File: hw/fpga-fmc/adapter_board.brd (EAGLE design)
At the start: 69 x 84 mm, 57 parts, among them J1 5569262-1, J2 ASP-134488-01, U1 ADM3066E, U2 ADM3066E, U3 ADM3066E, U4 ADM3066E, U5 ADM3066E, U6 ADM3066E

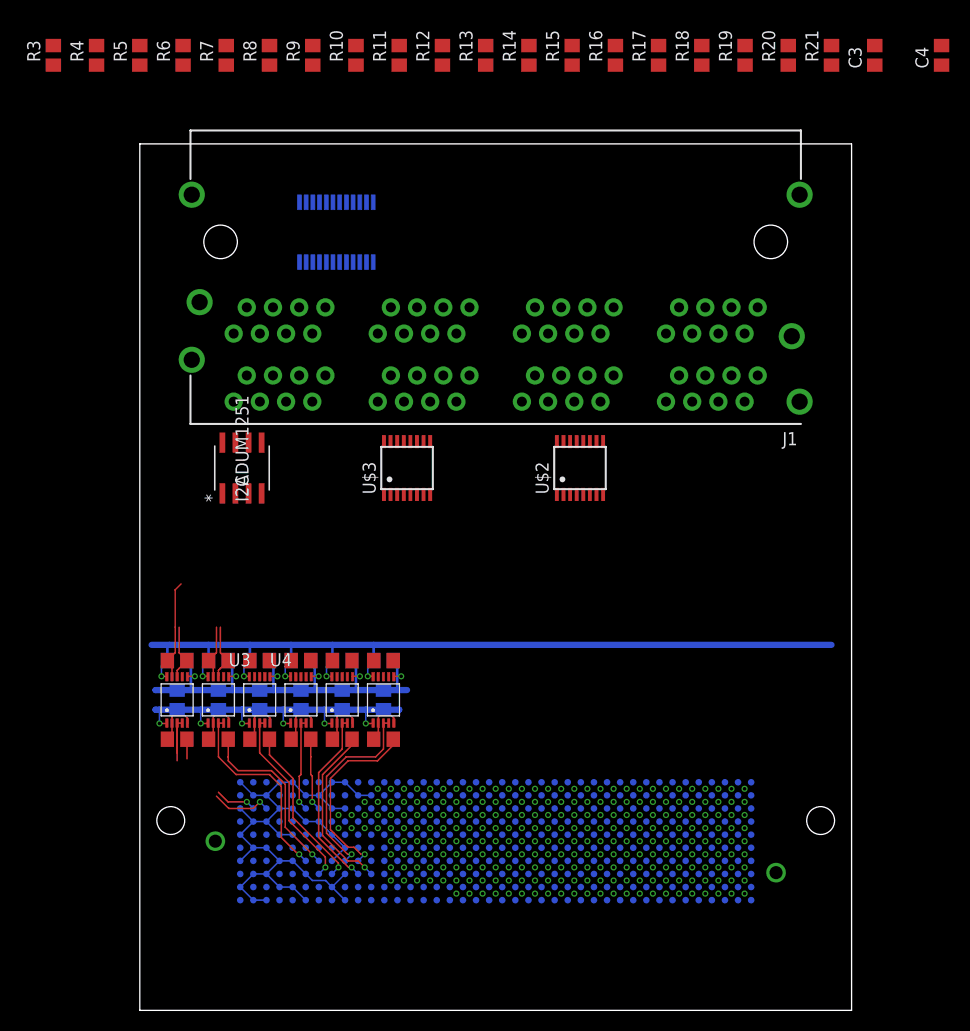
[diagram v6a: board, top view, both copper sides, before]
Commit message: fpga-fmc: add i2c circuit and level shifter for conv signal
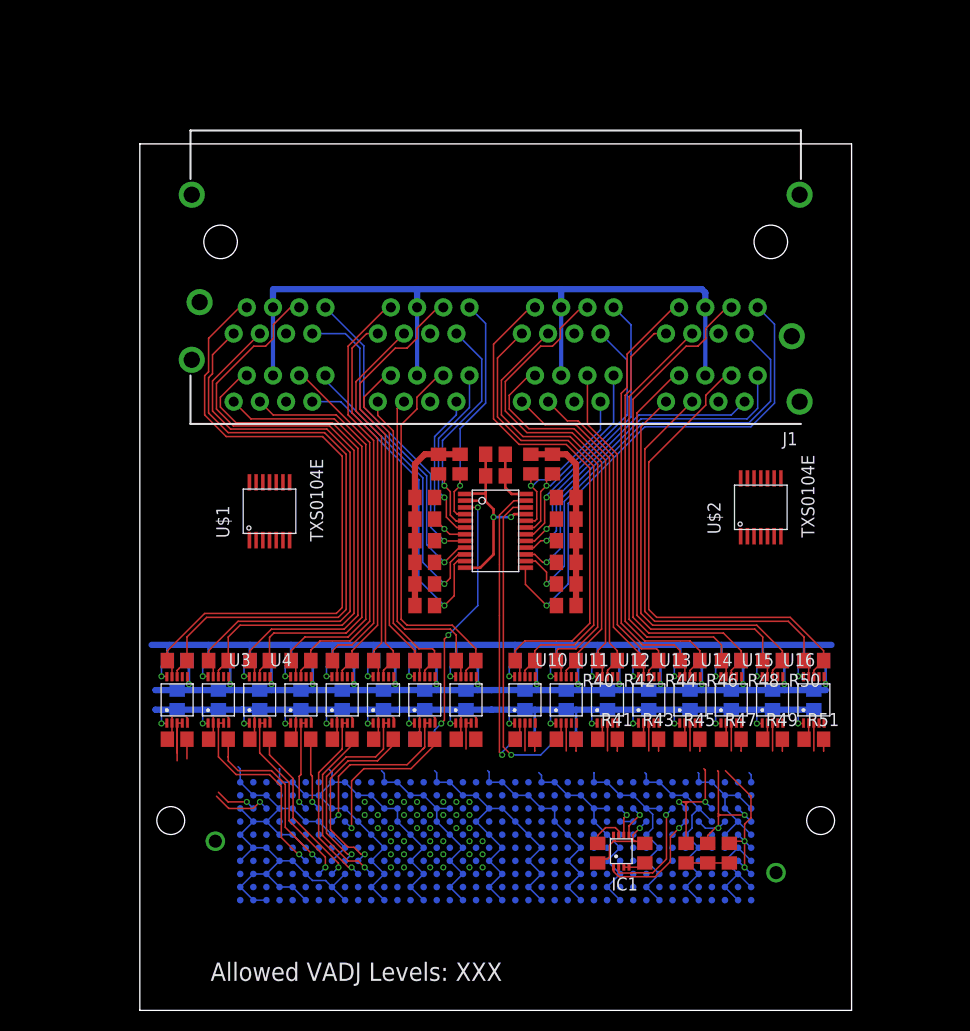
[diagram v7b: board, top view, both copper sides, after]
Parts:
- removed I2C: ADUM1251, ADUM1251WARZ:R_8_ADI
- removed U$3: ADUM140DQSOP-16, parts:QSOP16
- added C15, C16, C17, C18, C19, C20, C21, C22, C23, C24, C25, C26, C27, C28, C29, C30, C31, C32, C33, C34, C35, C36, C37, C39: 100n, rcl:C0805
- added IC1: M24C02, parts:8-VFSOP
- added R32, R34, R36, R38, R40, R42, R44, R46, R48, R50: (no value), rcl:R0805
- added R33, R35, R37, R39, R41, R43, R45, R47, R49, R51: 100R, rcl:R0805
- added R52: 0R, rcl:R0805
- added U10, U11, U12, U13, U14, U15, U16, U7, U8, U9: ADM3066E, parts:MSOP-10
- added U17: TCA9548A, parts:PCA9548
- R10, R11, R12, R13, R14, R15, R16, R17, R18, R19, R20, R21, R3, R4, R5, R6, R8, R9: value (none) -> 1k
- R7: value (none) -> 10k
- U$1: value PCA9548A -> TXS0104E; device parts:PCA9548 -> parts:TSSOP-14
- U$2: value ADUM140DQSOP-16 -> TXS0104E; device parts:QSOP16 -> parts:TSSOP-14
- moved R5 76.1 mm to (37.3, 26.3), flipped to the bottom, turned to 180 degrees
- moved R6 76.0 mm to (41.3, 26.3), flipped to the bottom, turned to 180 degrees
- moved R7 69.0 mm to (27.6, 26.3), flipped to the bottom, turned to 0 degrees
- moved C4 59.4 mm to (34.5, 51.8), turned to 0 degrees
- moved R3 55.9 mm to (31.1, 53.0)
- moved R13 53.7 mm to (27.6, 39.2), turned to 180 degrees
- moved R14 53.5 mm to (41.3, 39.2), turned to 0 degrees
- moved C3 53.4 mm to (34.5, 53.9), turned to 0 degrees
- moved R4 51.7 mm to (29.0, 53.0)
- moved R12 51.3 mm to (27.6, 41.3), turned to 180 degrees
- moved R15 51.2 mm to (41.3, 41.3), turned to 0 degrees
- moved R16 49.4 mm to (41.3, 43.4), turned to 0 degrees
- moved R11 49.2 mm to (27.6, 43.4), turned to 180 degrees
- moved R21 49.2 mm to (37.9, 53.0)
- moved R17 47.9 mm to (41.3, 45.5), turned to 0 degrees
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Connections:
- removed net 3V3: C3.2, C4.2, U$1.P23
- removed net N$18: R9.1, U$1.P6
- removed net N$19: R10.1, U$1.P7
- removed net N$20: R11.1, U$1.P8
- removed net N$21: U$1.P9
- removed net N$22: R12.1, R13.1, U$1.P10
- removed net N$23: R14.1, U$1.P12
- removed net N$24: R15.1, U$1.P13
- removed net N$25: R16.1, U$1.P14
- removed net N$30: R17.1, U$1.P15
- removed net N$38: R18.1, U$1.P16
- removed net N$41: R19.1, U$1.P17
- removed net N$42: R20.1, U$1.P18
- removed net N$43: R21.1, U$1.P19
- new net 3P3VAUX: C39.2, IC1.P8, J2.D32, R52.2
- new net GA0: IC1.P2, J2.C34
- new net GA1: IC1.P1, J2.D35
- new net LSIO10: R39.1, U10.P1, U10.P4
- new net LSIO11: R41.1, U11.P1, U11.P4
- new net LSIO12: R43.1, U12.P1, U12.P4
- new net LSIO13: R45.1, U13.P1, U13.P4
- new net LSIO14: R47.1, U14.P1, U14.P4
- new net LSIO15: R49.1, U15.P1, U15.P4
- new net LSIO16: R51.1, U16.P1, U16.P4
- new net LSIO7: R33.1, U7.P1, U7.P4
- new net LSIO8: R35.1, U8.P1, U8.P4
- new net LSIO9: R37.1, U9.P1, U9.P4
- new net N$10: U$2.10
- new net N$11: U$2.11
- new net N$12: U$2.12
- new net N$13: U$2.13
- new net N$15: U$1.11
- new net N$16: U$1.12
- new net N$17: U$1.13
- new net N$2: U$2.5
- new net N$3: U$2.4
- new net N$4: U$2.3
- new net N$5: U$2.2
- new net N$7: U$1.4
- new net N$8: U$1.3
- new net N$9: U$1.2
- net +12V: now also C37.2
- net +3V3: now also C36.2; no longer J2.D32
- net 0V: now also C15.2, C16.2, C17.2, C18.2, C19.2, C20.2, C21.2, C22.2, C23.2, C24.2, C25.2, C26.2, C27.2, C28.2, C29.2, C30.2, C31.2, C32.2, C33.2, C34.2, C35.1, C36.1, C37.1, C39.1, IC1.P3, IC1.P4, J2.401, J2.402, U$1.7, U$2.7, U10.P5, U11.P5, U12.P5, U13.P5, U14.P5, U15.P5, U16.P5, U17.P0, U17.P1, U17.P11, U17.P20, U7.P5, U8.P5, U9.P5; no longer J2.C34, J2.D35, U$1.P0, U$1.P1, U$1.P11, U$1.P20
- net 1V8: now also C15.1, C17.1, C19.1, C21.1, C23.1, C25.1, C27.1, C29.1, C3.2, C31.1, C33.1, C4.2, U$1.1, U$1.8, U$2.1, U$2.8, U10.P0, U11.P0, U12.P0, U13.P0, U14.P0, U15.P0, U16.P0, U17.P23, U7.P0, U8.P0, U9.P0
- net 5V: now also C16.1, C18.1, C20.1, C22.1, C24.1, C26.1, C28.1, C30.1, C32.1, C34.1, U$1.14, U$2.14, U10.P9, U11.P9, U12.P9, U13.P9, U14.P9, U15.P9, U16.P9, U7.P9, U8.P9, U9.P9
- net FMC_DP0_C2M_N: now also U9.P2, U9.P3
- net FMC_DP0_C2M_P: now also R37.2
- net FMC_DP0_M2C_N: now also R43.2
- net FMC_DP0_M2C_P: now also U12.P2, U12.P3
- net FMC_IIC_SCL: now also IC1.P6
- net FMC_IIC_SDA: now also IC1.P5
- net FMC_LA00_CC_N: now also R39.2
- net FMC_LA00_CC_P: now also U10.P2, U10.P3
- net FMC_LA01_CC_N: now also R33.2, R49.2
- net FMC_LA01_CC_P: now also U15.P2, U15.P3, U7.P2, U7.P3
- net FMC_LA02_N: now also R41.2
- net FMC_LA02_P: now also U11.P2, U11.P3
- net FMC_LA03_N: now also R35.2, R47.2, R51.2
- net FMC_LA03_P: now also U14.P2, U14.P3, U16.P2, U16.P3, U8.P2, U8.P3
- net FMC_LA04_N: now also R45.2
- net FMC_LA04_P: now also U13.P2, U13.P3
- net N$1: now also IC1.P7, R52.1; no longer R3.1, U$1.P3
- net N$14: now also U$1.10; no longer R8.1, U$1.P5
- net N$44: now also U17.P22; no longer U$1.P22
- net N$45: now also U17.P21; no longer U$1.P21
- net N$46: now also U17.P2; no longer U$1.P2
- net N$6: now also U$1.5; no longer R4.1, U$1.P4
- net RJ1_CLK_N: now also R48.2, U15.P8
- net RJ1_CLK_P: now also R48.1, U15.P7
- net RJ1_DATA_N: now also R50.2, U16.P8
- net RJ1_DATA_P: now also R50.1, U16.P7
- net RJ1_SCL: now also R17.1, U17.P15
- net RJ1_SDO: now also R16.1, U17.P14
- net RJ2_CLK_N: now also R40.2, U11.P8
- net RJ2_CLK_P: now also R40.1, U11.P7
- net RJ2_DATA_N: now also R42.2, U12.P8
- net RJ2_DATA_P: now also R42.1, U12.P7
- net RJ2_SCL: now also R21.1, U17.P19
- net RJ2_SDO: now also R20.1, U17.P18
- net RJ3_CLK_N: now also R32.2, U7.P8
- net RJ3_CLK_P: now also R32.1, U7.P7
- net RJ3_DATA_N: now also R34.2, U8.P8
- net RJ3_DATA_P: now also R34.1, U8.P7
- net RJ3_SCL: now also R9.1, U17.P6
- net RJ3_SDO: now also R8.1, U17.P5
- net RJ4_SCL: now also R13.1, U17.P10
- net RJ4_SDO: now also R12.1, U17.P9
- net RJ5_CLK_N: now also R44.2, U13.P8
- net RJ5_CLK_P: now also R44.1, U13.P7
- net RJ5_DATA_N: now also R46.2, U14.P8
- net RJ5_DATA_P: now also R46.1, U14.P7
- net RJ5_SCL: now also R15.1, U17.P13
- net RJ5_SDO: now also R14.1, U17.P12
- net RJ6_CLK_N: now also R36.2, U9.P8
- net RJ6_CLK_P: now also R36.1, U9.P7
- net RJ6_DATA_N: now also R38.2, U10.P8
- net RJ6_DATA_P: now also R38.1, U10.P7
- net RJ6_SCL: now also R19.1, U17.P17
- net RJ6_SDO: now also R18.1, U17.P16
- net RJ7_SCL: now also R4.1, U17.P4
- net RJ7_SDO: now also R3.1, U17.P3
- net RJ8_SCL: now also R11.1, U17.P8
- net RJ8_SDO: now also R10.1, U17.P7
- net V+: now also C35.2
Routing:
- net 0V: track 119.9 -> 415.7 mm, vias 6 -> 18
- net +12V: track 0.00 -> 87.4 mm, vias 0 -> 2
- net 5V: track 89.0 -> 164.4 mm, vias 6 -> 16
- net 1V8: track 36.0 -> 105.2 mm, vias 6 -> 16
- net RJ8_DATA_P: track 5.51 -> 62.5 mm
- net RJ8_CLK_P: track 5.51 -> 59.5 mm
- net RJ8_CLK_N: track 9.75 -> 63.6 mm
- net RJ8_DATA_N: track 5.32 -> 57.8 mm
- net RJ5_SDO: track 0.00 -> 50.2 mm, vias 0 -> 1
- net RJ4_CLK_N: track 0.00 -> 50.2 mm
- net RJ6_CLK_N: track 0.00 -> 50.1 mm
- net RJ5_DATA_P: track 0.00 -> 49.7 mm
- net RJ6_DATA_P: track 0.00 -> 48.0 mm
- net RJ1_DATA_P: track 0.00 -> 47.9 mm
- net RJ6_CLK_P: track 0.00 -> 45.4 mm
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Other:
- board text added: "Allowed VADJ Levels: XXX"

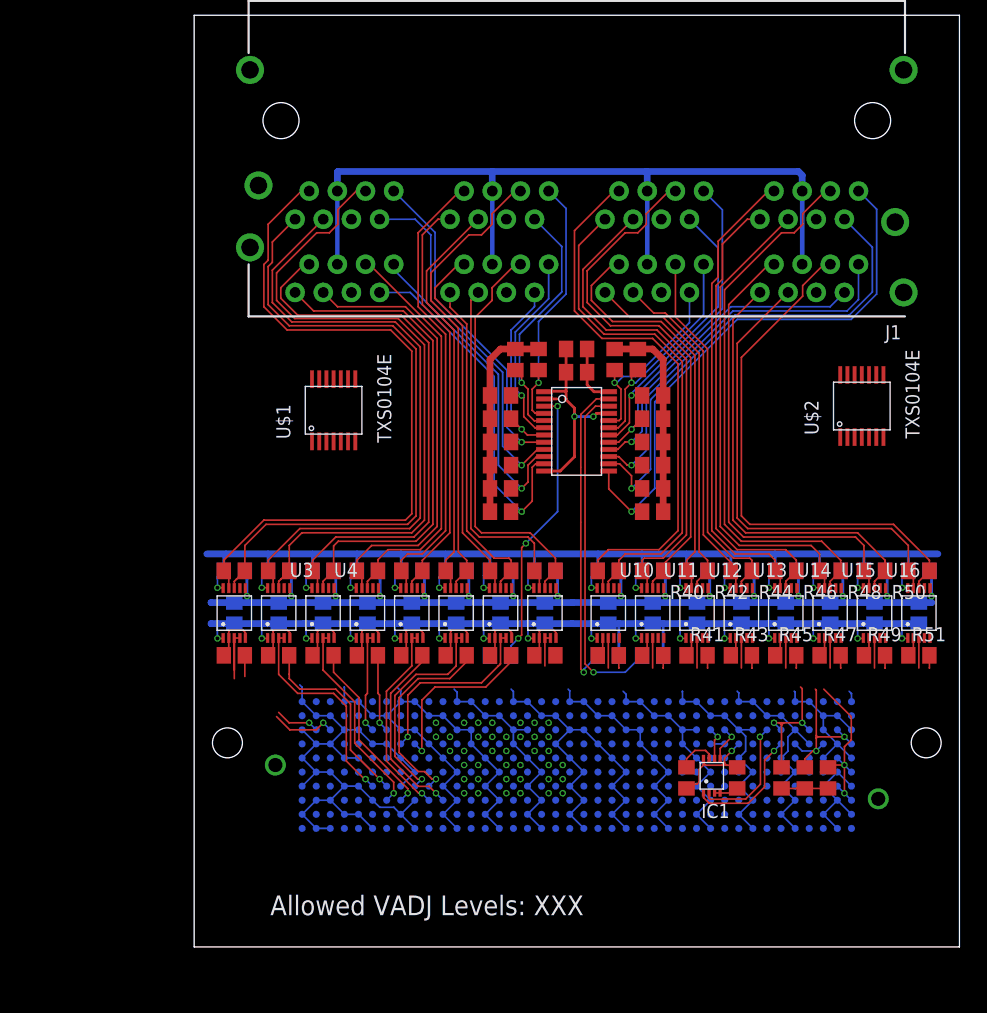
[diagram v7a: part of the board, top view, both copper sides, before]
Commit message: fpga_fmc: route conv signals and more rj channels
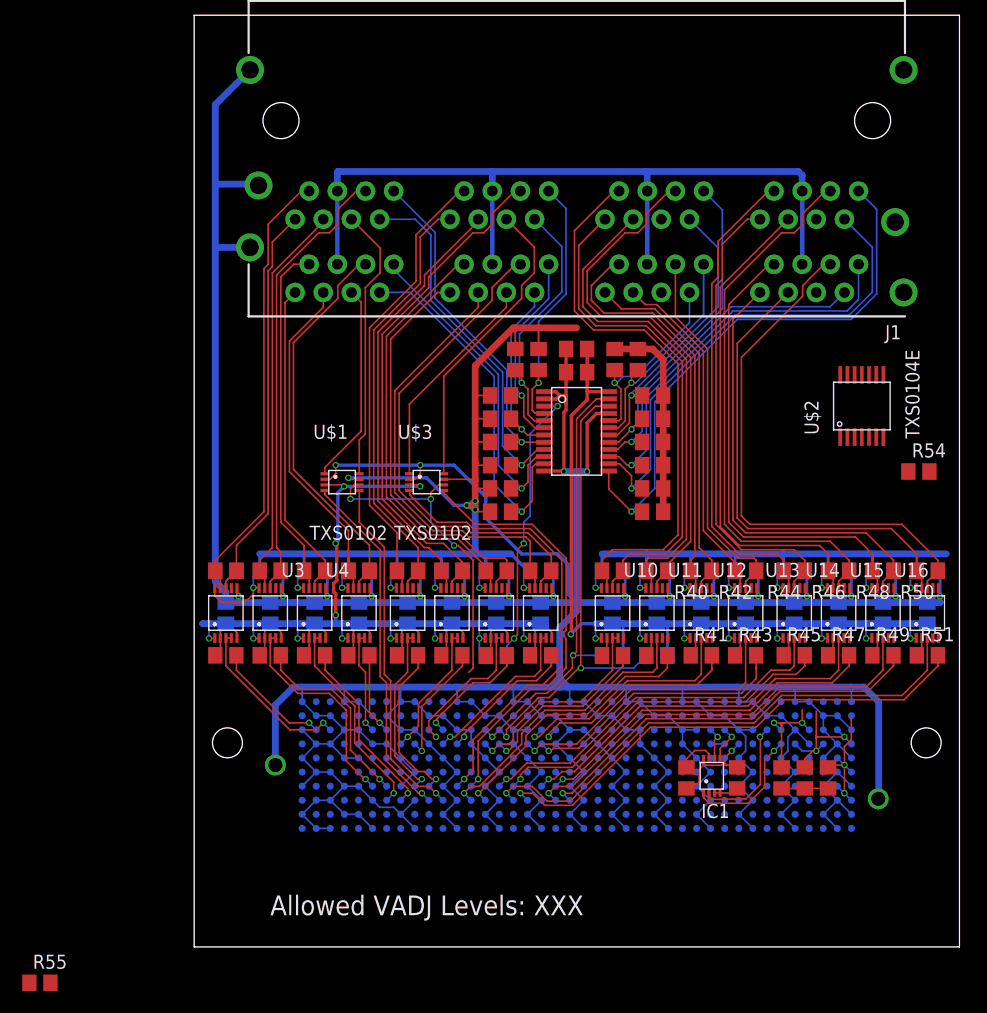
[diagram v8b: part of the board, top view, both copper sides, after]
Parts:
- added R54, R55: (no value), rcl:R0805
- added U$3: TXS0102, parts:VSSOP-8
- U$1: value TXS0104E -> TXS0102; device parts:TSSOP-14 -> parts:VSSOP-8
- moved U$1 6.52 mm to (13.3, 41.9), turned to 0 degrees
- moved C10 0.76 mm to (14.9, 33.9)
- moved C29 0.76 mm to (58.1, 30.1)
- moved C30 0.76 mm to (58.1, 33.9)
- moved C31 0.76 mm to (62.1, 30.1)
- moved C32 0.76 mm to (62.1, 33.9)
- moved C33 0.76 mm to (66.1, 30.1)
- moved C34 0.76 mm to (66.1, 33.9)
- moved C5 0.76 mm to (6.86, 30.1)
- moved C6 0.76 mm to (6.86, 33.9)
- moved C7 0.76 mm to (10.9, 30.1)
- moved C8 0.76 mm to (10.9, 33.9)
- moved C9 0.76 mm to (14.9, 30.1)
- moved R22 0.76 mm to (6.86, 33.9)
- moved R23 0.76 mm to (6.86, 26.3)
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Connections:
- net N$46 renamed I2C_RESET
- removed net N$10: U$2.10
- removed net N$11: U$2.11
- removed net N$12: U$2.12
- removed net N$14: U$1.10
- removed net N$15: U$1.11
- removed net N$16: U$1.12
- removed net N$17: U$1.13
- removed net N$44: R5.1, U17.P22
- removed net N$45: R6.1, U17.P21
- removed net N$6: U$1.5
- removed net N$7: U$1.4
- removed net N$8: U$1.3
- removed net N$9: U$1.2
- new net CONV_OE: R55.2, U$1.6, U$3.6
- net 0V: now also R54.1, R55.1, U$1.2, U$3.2; no longer U$1.7
- net 1V8: now also U$1.3, U$3.3; no longer U$1.1, U$1.8, U$2.8
- net 5V: now also U$1.7, U$3.7; no longer U$1.14
- net FMC_DP0_C2M_N: no longer U9.P2, U9.P3
- net FMC_DP0_C2M_P: no longer R37.2
- net FMC_DP0_M2C_N: no longer R43.2
- net FMC_DP0_M2C_P: no longer U12.P2, U12.P3
- net FMC_LA00_CC_N: no longer R39.2
- net FMC_LA00_CC_P: no longer U10.P2, U10.P3
- net FMC_LA01_CC_N: now also R31.2; no longer R33.2, R49.2
- net FMC_LA01_CC_P: now also U6.P2, U6.P3; no longer U15.P2, U15.P3, U7.P2, U7.P3
- net FMC_LA02_N: no longer R41.2
- net FMC_LA02_P: no longer U11.P2, U11.P3
- net FMC_LA03_N: now also R29.2; no longer R31.2, R35.2, R47.2, R51.2
- net FMC_LA03_P: now also U5.P2, U5.P3; no longer U14.P2, U14.P3, U16.P2, U16.P3, U6.P2, U6.P3, U8.P2, U8.P3
- net FMC_LA04_N: now also U$1.5; no longer R29.2, R45.2
- net FMC_LA04_P: now also U$1.4; no longer U13.P2, U13.P3, U5.P2, U5.P3
- net FMC_LA05_N: now also R35.2
- net FMC_LA05_P: now also U8.P2, U8.P3
- net FMC_LA06_N: now also R33.2
- net FMC_LA06_P: now also U7.P2, U7.P3
- net FMC_LA07_N: now also R39.2
- net FMC_LA07_P: now also U10.P2, U10.P3
- net FMC_LA08_N: now also U$3.5
- net FMC_LA08_P: now also U$3.4
- net FMC_LA09_N: now also R37.2
- net FMC_LA09_P: now also U9.P2, U9.P3
- net FMC_LA10_N: now also R6.1, U17.P21
- net FMC_LA10_P: now also R5.1, U17.P22
- net FMC_LA11_N: now also R51.2
- net FMC_LA11_P: now also U16.P2, U16.P3
- net FMC_LA12_N: now also R45.2
- net FMC_LA12_P: now also U13.P2, U13.P3
- net FMC_LA13_N: now also R43.2
- net FMC_LA13_P: now also U12.P2, U12.P3
- net FMC_LA14_N: now also R41.2
- net FMC_LA14_P: now also U11.P2, U11.P3
- net FMC_LA15_N: now also R49.2
- net FMC_LA15_P: now also U15.P2, U15.P3
- net FMC_LA16_N: now also R47.2
- net FMC_LA16_P: now also U14.P2, U14.P3
- net N$13: now also R54.2, U$2.8; no longer U$2.13
- net RJ1_CONV: now also U$2.10
- net RJ2_CONV: now also U$2.13
- net RJ3_CONV: now also U$3.1
- net RJ4_CONV: now also U$1.1
- net RJ5_CONV: now also U$2.11
- net RJ6_CONV: now also U$2.12
- net RJ7_CONV: now also U$3.8
- net RJ8_CONV: now also U$1.8
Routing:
- net 0V: track 415.7 -> 602.0 mm, vias 18 -> 20
- net FMC_LA11_P: track 0.00 -> 47.4 mm, vias 0 -> 1
- net 1V8: track 105.2 -> 151.6 mm, vias 16 -> 21
- net FMC_LA11_N: track 0.00 -> 45.1 mm, vias 0 -> 1
- net FMC_LA10_N: track 0.00 -> 42.3 mm, vias 0 -> 2
- net FMC_LA08_P: track 0.00 -> 41.8 mm, vias 0 -> 1
- net FMC_LA10_P: track 0.00 -> 39.6 mm, vias 0 -> 2
- net FMC_LA08_N: track 0.00 -> 38.7 mm, vias 0 -> 1
- net FMC_LA15_P: track 0.00 -> 38.5 mm, vias 0 -> 1
- net FMC_LA15_N: track 0.00 -> 36.4 mm, vias 0 -> 1
- net FMC_LA16_P: track 0.00 -> 34.0 mm, vias 0 -> 1
- net FMC_LA12_P: track 0.00 -> 33.6 mm, vias 0 -> 1
- net FMC_LA12_N: track 0.00 -> 31.9 mm, vias 0 -> 1
- net FMC_LA16_N: track 0.00 -> 31.9 mm, vias 0 -> 1
- net 5V: track 164.4 -> 195.8 mm, vias 16 -> 19
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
